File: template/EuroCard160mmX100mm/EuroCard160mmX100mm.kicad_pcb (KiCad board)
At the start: 2 copper layers, 159.8 x 99.8 mm, 0 parts

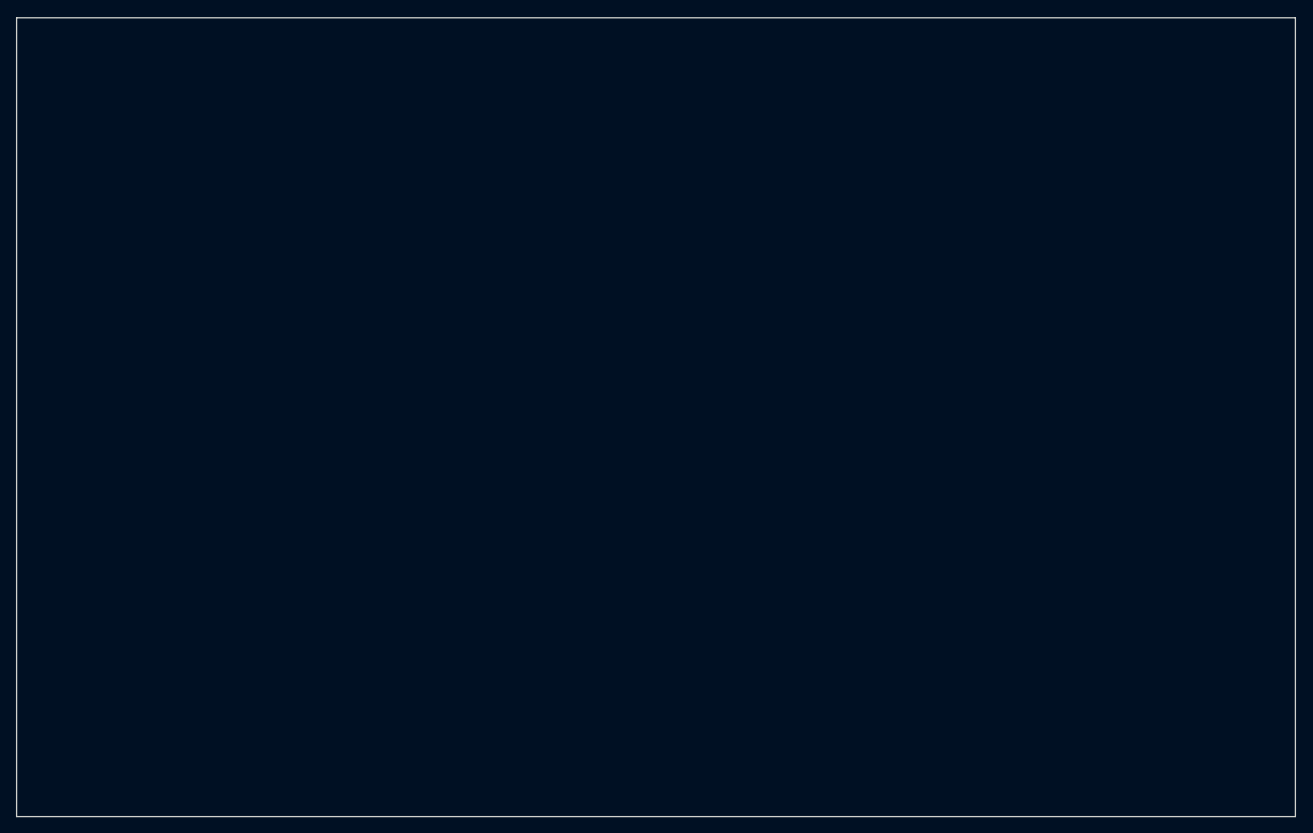
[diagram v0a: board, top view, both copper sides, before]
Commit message: fix: change original libs; add: new components
- Fix LIS3DH pins positions;
- Add ATmega164P symbol;
- Add 3D model to the L_Wuerth_HCM-7050;
- Add parameters for R_RES (Assembly...).
- Add parameters for R_RES and C_CAP;
- Fix SOIC-8 package 3D model;
- Add new parameters for many symbols;
- Change text height from 70 mil to 50 mil;
- Add solder mask expansion for 2-contact jumpers;
- Change thermopad vias of QFN-20-1EP_3x3mm_P0.45mm_EP1.6x1.6mm_ThermalVias;
- Add D_SMAF footprint;
- Fillet silk for C_1206;
-Rectangle silk for R_1206;
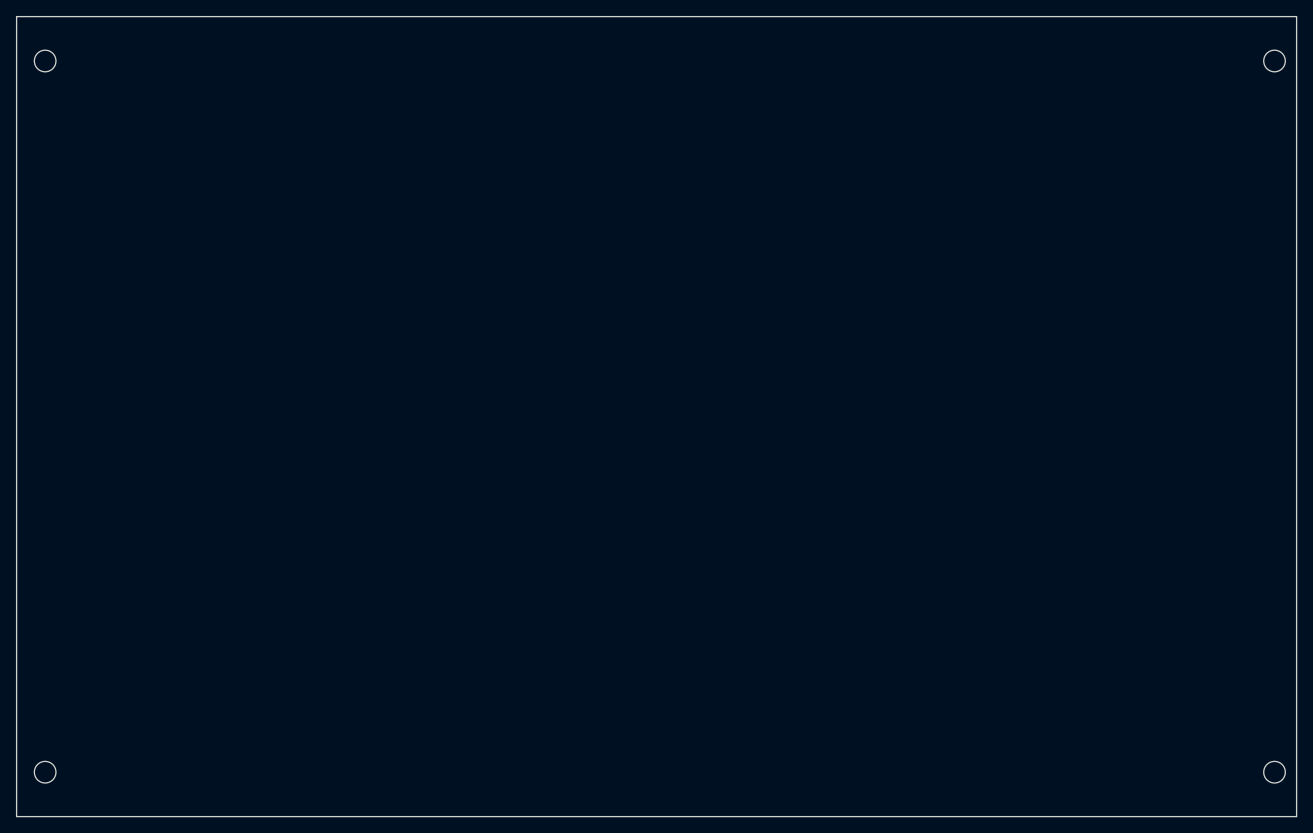
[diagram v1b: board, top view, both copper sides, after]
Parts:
- added MH1: MountingHole_2.7mm_M2.5_DIN965, MountingHole:MountingHole_2.7mm_M2.5_DIN965, F.Cu at (58.6, 50.5)
- added MH2: MountingHole_2.7mm_M2.5_DIN965, MountingHole:MountingHole_2.7mm_M2.5_DIN965, F.Cu at (58.6, 139.4)
- added MH3: MountingHole_2.7mm_M2.5_DIN965, MountingHole:MountingHole_2.7mm_M2.5_DIN965, F.Cu at (212.2, 50.5)
- added MH4: MountingHole_2.7mm_M2.5_DIN965, MountingHole:MountingHole_2.7mm_M2.5_DIN965, F.Cu at (212.2, 139.4)
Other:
- board size 159.8 x 99.8 mm -> 160 x 100 mm
- board text added: "Mounting holes are optional Keepout areas are for for guide rails"
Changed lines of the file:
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@@
-(kicad_pcb (version 20210126) (generator pcbnew)
+(kicad_pcb (version 20211014) (generator pcbnew)
   (general
     (thickness 1.6)
@@
   )
   (setup
+    (stackup
+      (layer "F.SilkS" (type "Top Silk Screen"))
+      (layer "F.Paste" (type "Top Solder Paste"))
+      (layer "F.Mask" (type "Top Solder Mask") (color "Green") (thickness 0.01))
+      (layer "F.Cu" (type "copper") (thickness 0.035))
+      (layer "dielectric 1" (type "core") (thickness 1.51) (material "FR4") (epsilon_r 4.5) (loss_tangent 0.02))
+      (layer "B.Cu" (type "copper") (thickness 0.035))
+      (layer "B.Mask" (type "Bottom Solder Mask") (color "Green") (thickness 0.01))
+      (layer "B.Paste" (type "Bottom Solder Paste"))
+      (layer "B.SilkS" (type "Bottom Silk Screen"))
+      (copper_finish "None")
+      (dielectric_constraints no)
+    )
+    (pad_to_mask_clearance 0)
+    (aux_axis_origin 55 145)
     (grid_origin 55 145)
     (pcbplotparams
@@
   )
   (net 0 "")
-  (gr_line (start 214.84 45.15) (end 55 45.15) (angle 90) (layer "Edge.Cuts") (width 0.15))
-  (gr_line (start 55 145) (end 214.85 145) (angle 90) (layer "Edge.Cuts") (width 0.15))
-  (gr_line (start 214.85 145) (end 214.85 45.15) (angle 90) (layer "Edge.Cuts") (width 0.15))
-  (gr_line (start 55 45.15) (end 55 145) (angle 90) (layer "Edge.Cuts") (width 0.15))
+  (footprint "MountingHole:MountingHole_2.7mm_M2.5_DIN965" locked (layer "F.Cu")
+    (at 212.24 139.45)
+    (descr "Mounting Hole 2.7mm, no annular, M2.5, DIN965")
+    (tags "mounting hole 2.7mm no annular m2.5 din965")
+    (attr exclude_from_pos_files exclude_from_bom)
+    (fp_text reference "MH4" (at 0 -3.35) (layer "F.SilkS") hide
+      (effects (font (size 1 1) (thickness 0.15)))
+    )
+    (fp_text value "MountingHole_2.7mm_M2.5_DIN965" (at 0 3.35) (layer "F.Fab") hide
+      (effects (font (size 1 1) (thickness 0.15)))
+    )
+    (fp_text user "${REFERENCE}" (at 0.3 0) (layer "F.Fab") hide
+      (effects (font (size 1 1) (thickness 0.15)))
+    )
+    (fp_circle (center 0 0) (end 2.35 0) (layer "Cmts.User") (width 0.15) (fill none))
+    (fp_circle (center 0 0) (end 2.6 0) (layer "F.CrtYd") (width 0.05) (fill none))
+    (pad "" np_thru_hole circle locked (at 0 0) (size 2.7 2.7) (drill 2.7) (layers *.Cu *.Mask))
+  )
+  (footprint "MountingHole:MountingHole_2.7mm_M2.5_DIN965" (layer "F.Cu")
+    (at 58.57 50.55)
+    (descr "Mounting Hole 2.7mm, no annular, M2.5, DIN965")
+    (tags "mounting hole 2.7mm no annular m2.5 din965")
+    (attr exclude_from_pos_files exclude_from_bom)
+    (fp_text reference "MH1" (at 0 -3.35) (layer "F.SilkS") hide
+      (effects (font (size 1 1) (thickness 0.15)))
+    )
+    (fp_text value "MountingHole_2.7mm_M2.5_DIN965" (at 0 3.35) (layer "F.Fab") hide
+      (effects (font (size 1 1) (thickness 0.15)))
+    )
+    (fp_text user "${REFERENCE}" (at 0.3 0) (layer "F.Fab") hide
+      (effects (font (size 1 1) (thickness 0.15)))
+    )
+    (fp_circle (center 0 0) (end 2.35 0) (layer "Cmts.User") (width 0.15) (fill none))
+    (fp_circle (center 0 0) (end 2.6 0) (layer "F.CrtYd") (width 0.05) (fill none))
+    (pad "" np_thru_hole circle locked (at 0 0) (size 2.7 2.7) (drill 2.7) (layers *.Cu *.Mask))
+  )
+  (footprint "MountingHole:MountingHole_2.7mm_M2.5_DIN965" locked (layer "F.Cu")
+    (at 58.57 139.45)
+    (descr "Mounting Hole 2.7mm, no annular, M2.5, DIN965")
+    (tags "mounting hole 2.7mm no annular m2.5 din965")
+    (attr exclude_from_pos_files exclude_from_bom)
+    (fp_text reference "MH2" (at 0 -3.35) (layer "F.SilkS") hide
+      (effects (font (size 1 1) (thickness 0.15)))
+    )
+    (fp_text value "MountingHole_2.7mm_M2.5_DIN965" (at 0 3.35) (layer "F.Fab") hide
+      (effects (font (size 1 1) (thickness 0.15)))
+    )
+    (fp_text user "${REFERENCE}" (at 0.3 0) (layer "F.Fab") hide
+      (effects (font (size 1 1) (thickness 0.15)))
+    )
+    (fp_circle (center 0 0) (end 2.35 0) (layer "Cmts.User") (width 0.15) (fill none))
+    (fp_circle (center 0 0) (end 2.6 0) (layer "F.CrtYd") (width 0.05) (fill none))
+    (pad "" np_thru_hole circle locked (at 0 0) (size 2.7 2.7) (drill 2.7) (layers *.Cu *.Mask))
+  )
+  (footprint "MountingHole:MountingHole_2.7mm_M2.5_DIN965" locked (layer "F.Cu")
+    (at 212.24 50.55)
+    (descr "Mounting Hole 2.7mm, no annular, M2.5, DIN965")
+    (tags "mounting hole 2.7mm no annular m2.5 din965")
+    (attr exclude_from_pos_files exclude_from_bom)
+    (fp_text reference "MH3" (at 0 -3.35) (layer "F.SilkS") hide
+      (effects (font (size 1 1) (thickness 0.15)))
+    )
+    (fp_text value "MountingHole_2.7mm_M2.5_DIN965" (at 0 3.35) (layer "F.Fab") hide
+      (effects (font (size 1 1) (thickness 0.15)))
+    )
+    (fp_text user "${REFERENCE}" (at 0.3 0) (layer "F.Fab") hide
+      (effects (font (size 1 1) (thickness 0.15)))
+    )
+    (fp_circle (center 0 0) (end 2.35 0) (layer "Cmts.User") (width 0.15) (fill none))
+    (fp_circle (center 0 0) (end 2.6 0) (layer "F.CrtYd") (width 0.05) (fill none))
+    (pad "" np_thru_hole circle locked (at 0 0) (size 2.7 2.7) (drill 2.7) (layers *.Cu *.Mask))
+  )
+  (gr_rect locked (start 55 145) (end 215 45) (layer "Edge.Cuts") (width 0.15) (fill none))
+  (gr_text "Mounting holes are optional\nKeepout areas are for for guide rails" (at 55.5 148) (layer "Cmts.User")
+    (effects (font (size 1 1) (thickness 0.15)) (justify left))
+  )
+  (zone (net 0) (net_name "") (layers F&B.Cu) (hatch full 0.508)
+    (connect_pads (clearance 0))
+    (min_thickness 0.254)
+    (keepout (tracks not_allowed) (vias not_allowed) (pads not_allowed ) (copperpour allowed) (footprints not_allowed))
+    (fill (thermal_gap 0.508) (thermal_bridge_width 0.508))
+    (polygon
+      (pts
+        (xy 215 145)
+        (xy 55 145)
+        (xy 55 142.5)
+        (xy 215 142.5)
+      )
+    )
+  )
+  (zone (net 0) (net_name "") (layers F&B.Cu) (hatch full 0.508)
+    (connect_pads (clearance 0))
+    (min_thickness 0.254)
+    (keepout (tracks not_allowed) (vias not_allowed) (pads not_allowed ) (copperpour allowed) (footprints not_allowed))
+    (fill (thermal_gap 0.508) (thermal_bridge_width 0.508))
+    (polygon
+      (pts
+        (xy 215 47.5)
+        (xy 55 47.5)
+        (xy 55 45)
+        (xy 215 45)
+      )
+    )
+  )
 )
